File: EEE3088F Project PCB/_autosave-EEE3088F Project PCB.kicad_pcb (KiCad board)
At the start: 2 copper layers, 80 x 54.9 mm, 76 parts, among them IC1 74LVC1G04SE-7, J1 JST PH 2.00mm connector, SW1 SS-12D10L3, U1 DRV8833PWR, U10 LM7805L-TF3-T, U11 TC4056A., U2 DRV8833PWPR, U3 INA219AxD, U4 CH224K, U6 MIC5504-1.2YM5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

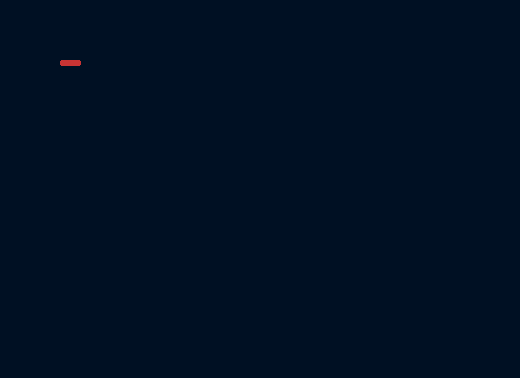
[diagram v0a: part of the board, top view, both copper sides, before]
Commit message: Adjusted arrangments on board, and assigned all JLCP part numbers
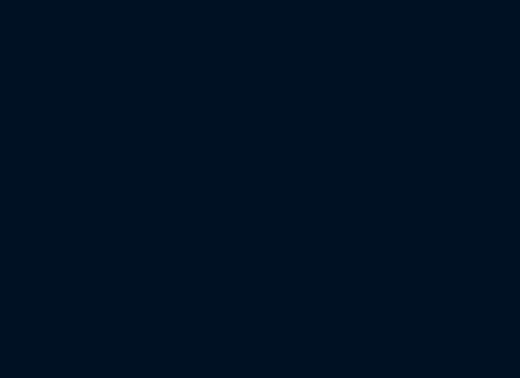
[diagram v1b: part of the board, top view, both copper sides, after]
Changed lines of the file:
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@@
 			)
 		)
-		(property "LCSC" "C4211"
+		(property "LCSC" "C22978"
 			(at 0 0 0)
 			(layer "F.SilkS")
@@
 			)
 		)
-		(property "LCSC" "C4211"
+		(property "LCSC" "C22978"
 			(at 0 0 0)
 			(layer "F.SilkS")
@@
 		)
 	)
-	(gr_rect
-		(start 59.75 62.775)
-		(end 60.25 62.775)
-		(stroke
-			(width 0.2)
-			(type default)
-		)
-		(fill no)
-		(layer "F.Cu")
-		(net 25)
-	)
 	(gr_arc
